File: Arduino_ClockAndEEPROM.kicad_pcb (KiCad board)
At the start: 2 copper layers, 39.9 x 25.9 mm, 17 parts, among them J1 Serial, J2 Digital pins, J3 ICSP, J4 I2C, U1 24LC1025, U2 24LC1025, U3 DS1337S+, U4 ATmega328P-AU, Y1 Xtal 32MHz, Y2 Xtal 16MHz

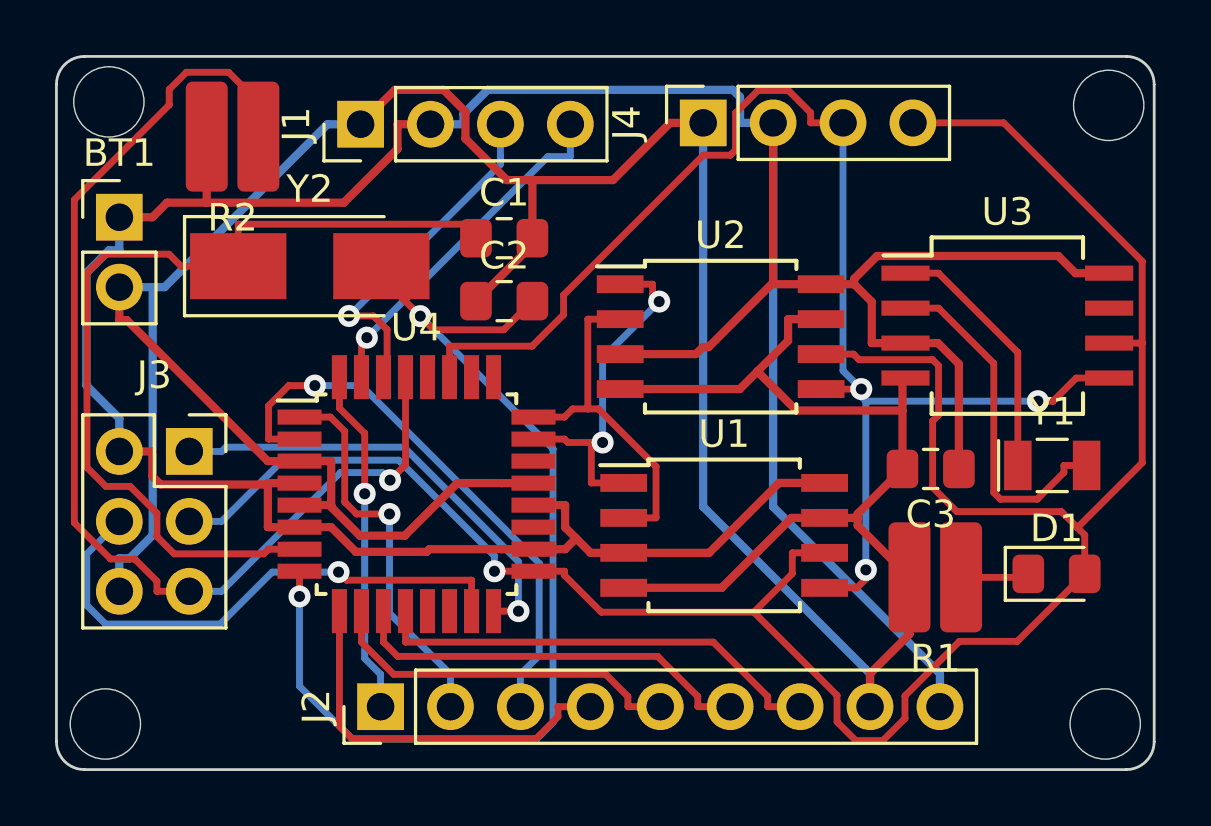
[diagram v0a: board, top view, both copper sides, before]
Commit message: Silkscreen and graphics added, PCB layout finalized.
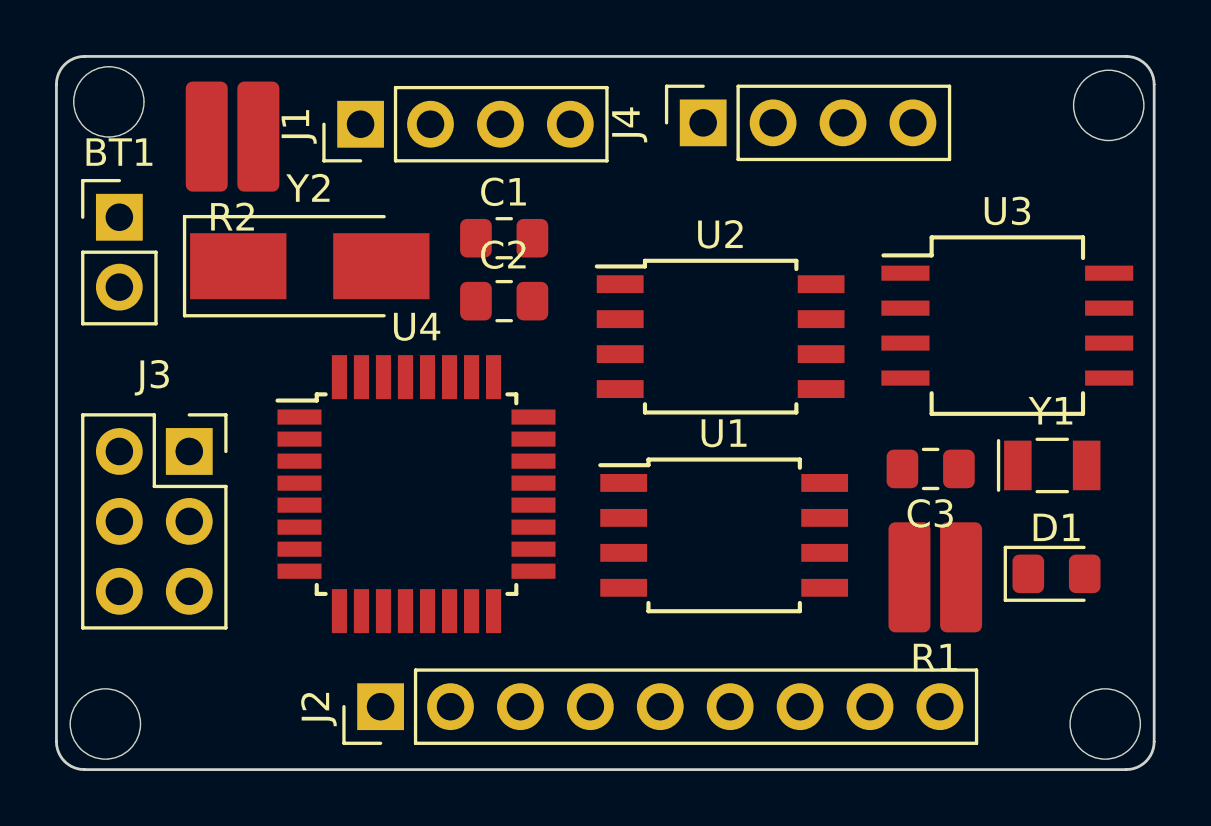
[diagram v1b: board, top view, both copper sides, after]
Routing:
- net /Vcc: track 132.2 -> 0.00 mm
- net GNDPWR: track 128.4 -> 0.00 mm
- net /SCK: track 84.4 -> 0.00 mm, vias 1 -> 0
- net /SDA: track 50.4 -> 0.00 mm, vias 3 -> 0
- net /RESET: track 41.0 -> 0.00 mm, vias 1 -> 0
- net Net-(C2-Pad2): track 38.3 -> 0.00 mm, vias 2 -> 0
- net Net-(C1-Pad1): track 33.0 -> 0.00 mm
- net /D4: track 20.6 -> 0.00 mm, vias 1 -> 0
- net /MOSI: track 19.8 -> 0.00 mm, vias 1 -> 0
- net /D8: track 16.6 -> 0.00 mm
- net /MISO: track 16.4 -> 0.00 mm, vias 1 -> 0
- net /D7: track 14.9 -> 0.00 mm
- net /D5: track 14.2 -> 0.00 mm
- net /D3: track 14.2 -> 0.00 mm, vias 1 -> 0
- net /D6: track 13.2 -> 0.00 mm
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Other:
- copper layers 2 -> 4
